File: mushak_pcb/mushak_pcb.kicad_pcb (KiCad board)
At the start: 2 copper layers, 57.7 x 40 mm, 115 parts, among them IC1 AS5600-ASOT, IC2 AS5600-ASOT, J1 Conn_01x04_Male, J10 IR_1, J11 AS5600_1, J12 IR_2, J13 AS5600_2, J14 IR_3, J15 ToF, J16 IR_4, J17 ToF, J2 Conn_01x02_Female, J3 BLE_Conn, J4 AS5600_Left, J5 AS5600_Right, J6 IR_1, J7 IR_3, J8 IR_2, J9 IR_4, M1 motor, M2 motor, Q1 DMN3065LW-7, Q2 DMN3065LW-7, Q3 DMN3065LW-7, Q4 DMN3065LW-7, Q5 DMN3065LW-7, SW1 SW_Push, SW2 SW_Push, U1 BA30BC0FP-E2, U3 DRV8833PW, U4 VL6180XV0NR/1, U5 MPU-6500, U6 STM32F405RGTx, Y1 25Mhz, Y2 32.769kHz

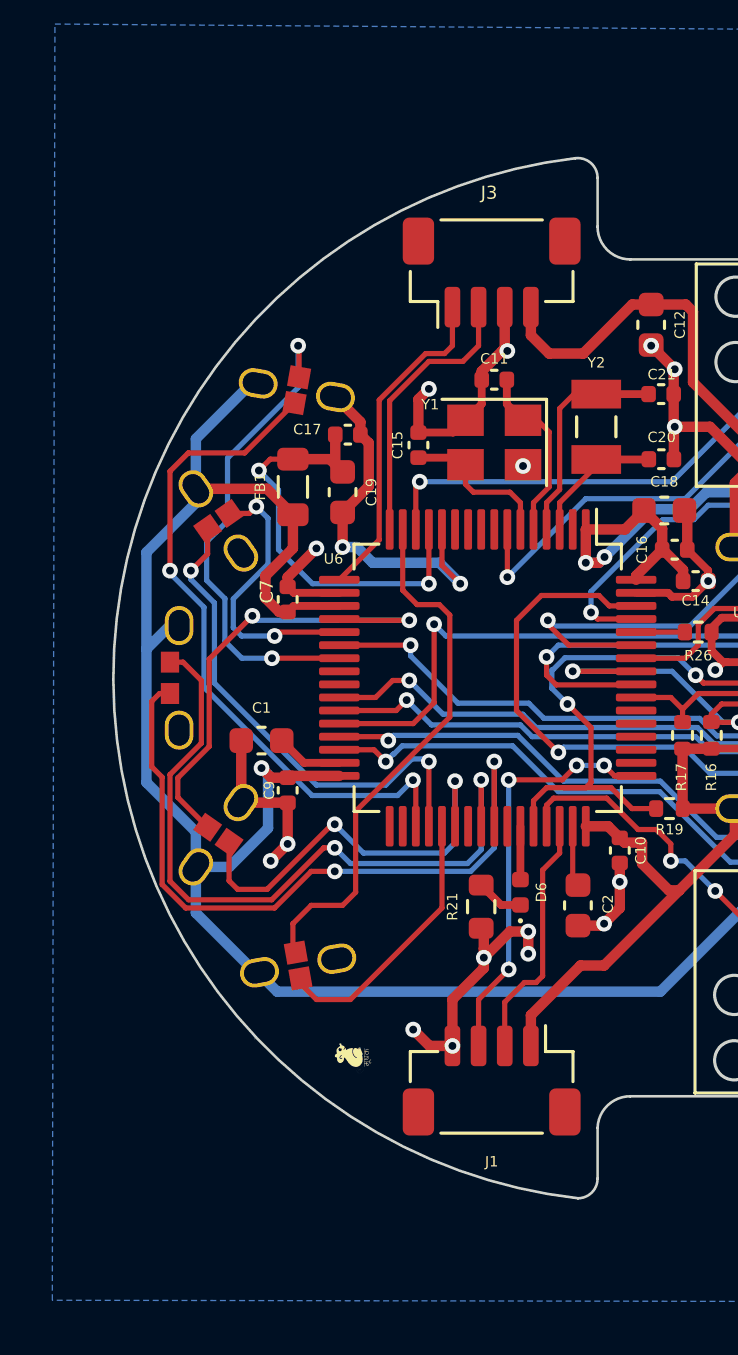
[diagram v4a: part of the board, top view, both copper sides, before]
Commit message: Updated graphics and added dimensions
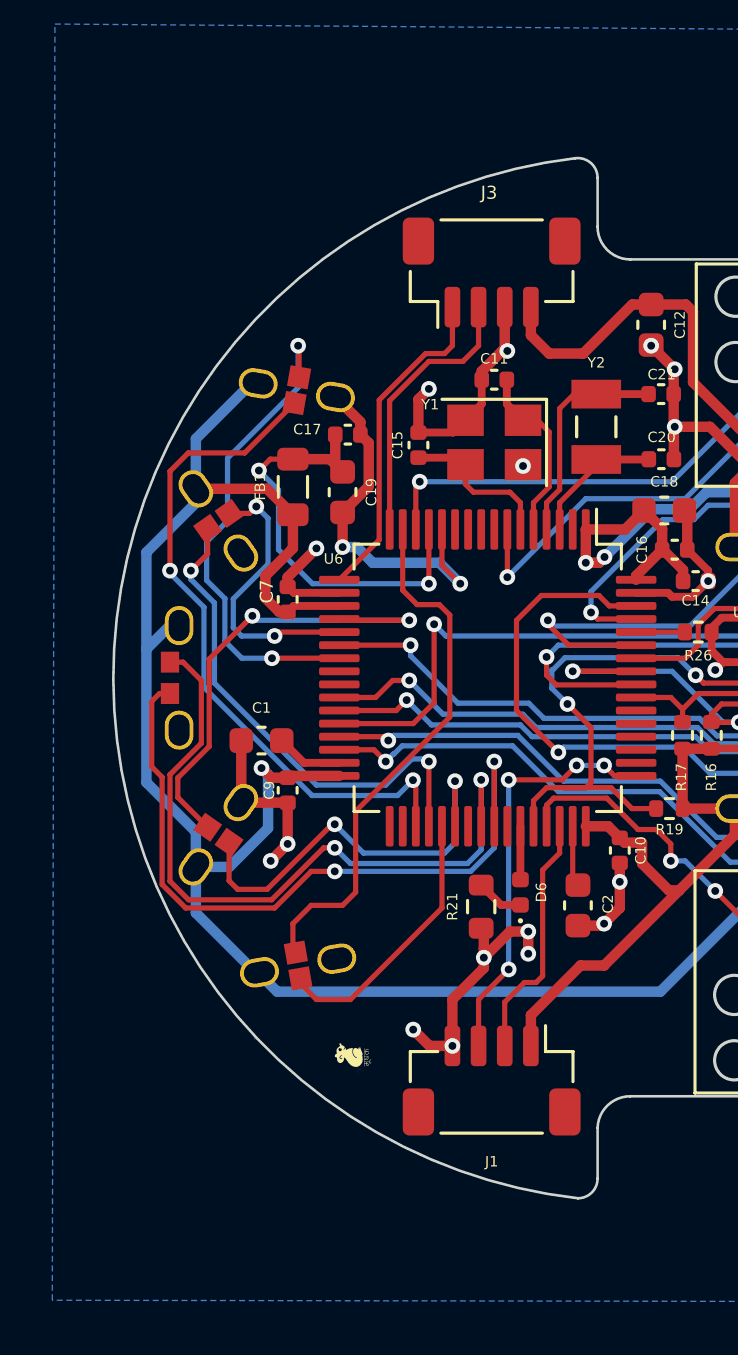
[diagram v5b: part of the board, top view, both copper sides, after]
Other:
- board text added: "SRA-VJTI"
- board text added: "Society of Robotics and Automation"
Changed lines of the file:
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@@
     (attr board_only exclude_from_pos_files exclude_from_bom)
     (fp_text reference "G***" (at 0.7 -3.75 90) (layer "F.SilkS")
-      (effects (font (size 0.05 0.05)))
+      (effects (font (size 0.05 0.05) (thickness 0.15)))
     )
     (fp_text value "LOGO" (at 0.75 0 90) (layer "F.SilkS") hide
@@
     (pad "8" smd rect locked (at 2.7 -1.905) (size 1.5 0.65) (layers "F.Cu" "F.Paste" "F.Mask")
       (net 18 "/AS5600_Right/GND_s") (pinfunction "DIR") (pintype "bidirectional"))
+    (model "${KIPRJMOD}/3d_models/AS5600/AS5600.stp"
+      (offset (xyz 0 0 0))
+      (scale (xyz 1 1 1))
+      (rotate (xyz 0 0 0))
+    )
   )
   (footprint "Capacitor_SMD:C_0402_1005Metric" (layer "F.Cu")
@@
       (net 100 "Net-(M1-Pad2)") (pinfunction "VMOT-") (pintype "input"))
     (model "${KIPRJMOD}/component_libraries/mushak_mount_footprint/L_Assem.STEP"
-      (offset (xyz 3 -36.5 -21))
+      (offset (xyz 3 -36.5 -21.5))
       (scale (xyz 1 1 1))
       (rotate (xyz -90 0 180))
@@
     (pad "8" smd rect locked (at 2.7 -1.905) (size 1.5 0.65) (layers "F.Cu" "F.Paste" "F.Mask")
       (net 31 "/AS5600_Left/+3V0_s") (pinfunction "DIR") (pintype "bidirectional"))
+    (model "${KIPRJMOD}/3d_models/AS5600/AS5600.stp"
+      (offset (xyz 0 0 0))
+      (scale (xyz 1 1 1))
+      (rotate (xyz 0 0 0))
+    )
   )
   (footprint "mushak_mount_footprint:IR_SLAVE_V_04" (layer "F.Cu")
@@
       (net 102 "Net-(M2-Pad2)") (pinfunction "VMOT-") (pintype "input"))
     (model "${KIPRJMOD}/component_libraries/mushak_mount_footprint/R_Assem.STEP"
-      (offset (xyz -29.5 -36.5 19.5))
+      (offset (xyz -29.5 -36.5 20.5))
       (scale (xyz 1 1 1))
       (rotate (xyz 90 0 0))
@@
   (gr_line (start 205.85 106.85) (end 204.75 106.85) (layer "Edge.Cuts") (width 0.1))
   (gr_line (start 204.85 112) (end 204.85 111.4) (layer "Edge.Cuts") (width 0.1))
-  (gr_arc (start 166 116.9) (mid 148.233702 97.059712) (end 165.9 77.13033) (layer "Edge.Cuts") (width 0.1))
+  (gr_arc (start 166 116.9) (mid 148.233259 97.059714) (end 165.9 77.13033) (layer "Edge.Cuts") (width 0.1))
   (gr_line (start 205.35 112.4) (end 205.35 115.2) (layer "Edge.Cuts") (width 0.1))
   (gr_line (start 205.4 98.8) (end 205.4 96.9) (layer "Edge.Cuts") (width 0.1))
@@
   (gr_line (start 206 65) (end 142.5 1.5) (layer "User.4") (width 0.15))
   (gr_line (start 142.5 128.5) (end 79 192) (layer "User.4") (width 0.15))
+  (gr_text "Society of Robotics and Automation" (at 186.15 97.65 90) (layer "B.SilkS")
+    (effects (font (size 0.7 0.7) (thickness 0.1)) (justify mirror))
+  )
   (gr_text "Designed by - Chinmay Lonkar" (at 190.9 96.6 90) (layer "B.SilkS")
     (effects (font (size 0.6 0.6) (thickness 0.08)) (justify mirror))
   )
+  (gr_text "SRA-VJTI" (at 188.65 97.05 90) (layer "B.SilkS")
+    (effects (font (size 1 1) (thickness 0.25)) (justify mirror))
+  )
+  (dimension (type aligned) (layer "Eco2.User")
+    (pts (xy 192.828427 78.171573) (xy 190 81))
+    (height 7.495331)
+    (gr_text "4.0000 mm" (at 185.301042 73.472614 45) (layer "Eco2.User")
+      (effects (font (size 1 1) (thickness 0.15)))
+    )
+    (format (units 3) (units_format 1) (precision 4))
+    (style (thickness 0.15) (arrow_length 1.27) (text_position_mode 0) (extension_height 0.58642) (extension_offset 0.5) keep_text_aligned)
+  )
+  (dimension (type aligned) (layer "Eco2.User")
+    (pts (xy 194 97) (xy 148.233702 97.059712))
+    (height 25.057386)
+    (gr_text "45.7663 mm" (at 171.082658 70.822492 0.07475465123) (layer "Eco2.User")
+      (effects (font (size 1 1) (thickness 0.15)))
+    )
+    (format (units 3) (units_format 1) (precision 4))
+    (style (thickness 0.15) (arrow_length 1.27) (text_position_mode 0) (extension_height 0.58642) (extension_offset 0.5) keep_text_aligned)
+  )
+  (dimension (type aligned) (layer "Eco2.User")
+    (pts (xy 148.233259 97.059714) (xy 168.3 97))
+    (height 26.007919)
+    (gr_text "20.0668 mm" (at 158.3406 121.887666 0.1704985503) (layer "Eco2.User")
+      (effects (font (size 1 1) (thickness 0.15)))
+    )
+    (format (units 3) (units_format 1) (precision 4))
+    (style (thickness 0.15) (arrow_length 1.27) (text_position_mode 0) (extension_height 0.58642) (extension_offset 0.5) keep_text_aligned)
+  )
+  (dimension (type aligned) (layer "Eco2.User")
+    (pts (xy 177.075 87.425) (xy 194 87.4))
+    (height -24.400859)
+    (gr_text "16.9250 mm" (at 185.499758 61.861669 0.08463181365) (layer "Eco2.User")
+      (effects (font (size 1 1) (thickness 0.15)))
+    )
+    (format (units 3) (units_format 1) (precision 4))
+    (style (thickness 0.15) (arrow_length 1.27) (text_position_mode 0) (extension_height 0.58642) (extension_offset 0.5) keep_text_aligned)
+  )
+  (dimension (type aligned) (layer "Eco2.User")
+    (pts (xy 177.075 86.925) (xy 182.575 86.925))
+    (height -17.975)
+    (gr_text "5.5000 mm" (at 179.825 67.8) (layer "Eco2.User")
+      (effects (font (size 1 1) (thickness 0.15)))
+    )
+    (format (units 3) (units_format 1) (precision 4))
+    (style (thickness 0.15) (arrow_length 1.27) (text_position_mode 0) (extension_height 0.58642) (extension_offset 0.5) keep_text_aligned)
+  )
+  (dimension (type aligned) (layer "Eco2.User")
+    (pts (xy 166.494225 77.313541) (xy 165.9941 77.8803))
+    (height 4.543301)
+    (gr_text "0.7559 mm" (at 161.975273 73.829925 48.57386691) (layer "Eco2.User")
+      (effects (font (size 1 1) (thickness 0.15)))
+    )
+    (format (units 3) (units_format 1) (precision 4))
+    (style (thickness 0.15) (arrow_length 1.27) (text_position_mode 0) (extension_height 0.58642) (extension_offset 0.5) keep_text_aligned)
+  )
+  (dimension (type aligned) (layer "Eco2.User")
+    (pts (xy 166.75 79.6) (xy 181.25 79.6))
+    (height -5.05)
+    (gr_text "14.5000 mm" (at 174 73.4) (layer "Eco2.User")
+      (effects (font (size 1 1) (thickness 0.15)))
+    )
+    (format (units 3) (units_format 1) (precision 4))
+    (style (thickness 0.15) (arrow_length 1.27) (text_position_mode 0) (extension_height 0.58642) (extension_offset 0.5) keep_text_aligned)
+  )
+  (dimension (type aligned) (layer "Eco2.User")
+    (pts (xy 186 77) (xy 186 117))
+    (height -28)
+    (gr_text "40.0000 mm" (at 212.85 97 90) (layer "Eco2.User")
+      (effects (font (size 1 1) (thickness 0.15)))
+    )
+    (format (units 3) (units_format 1) (precision 4))
+    (style (thickness 0.15) (arrow_length 1.27) (text_position_mode 0) (extension_height 0.58642) (extension_offset 0.5) keep_text_aligned)
+  )
   (segment (start 197.95 105.2) (end 196.15 103.4) (width 0.2) (layer "F.Cu") (net 1))

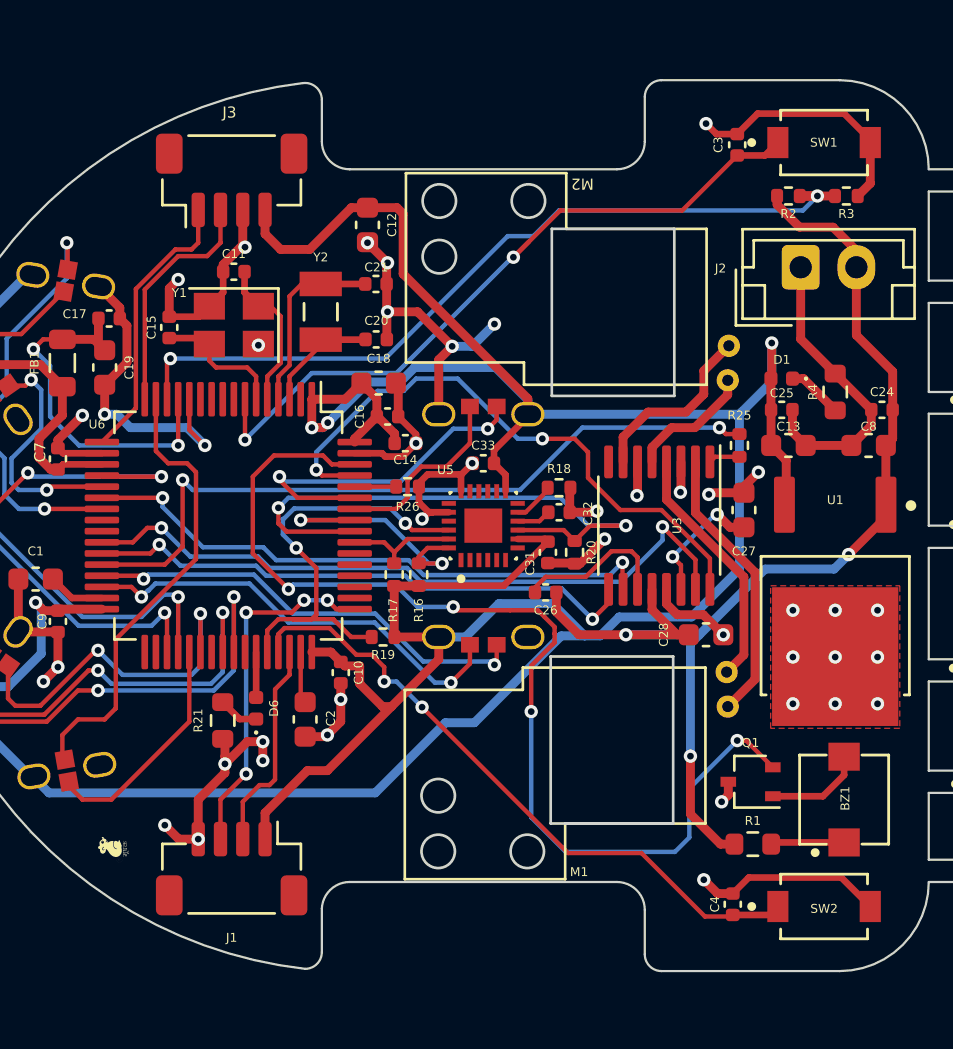
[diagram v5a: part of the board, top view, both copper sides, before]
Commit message: changed oscilattor placement
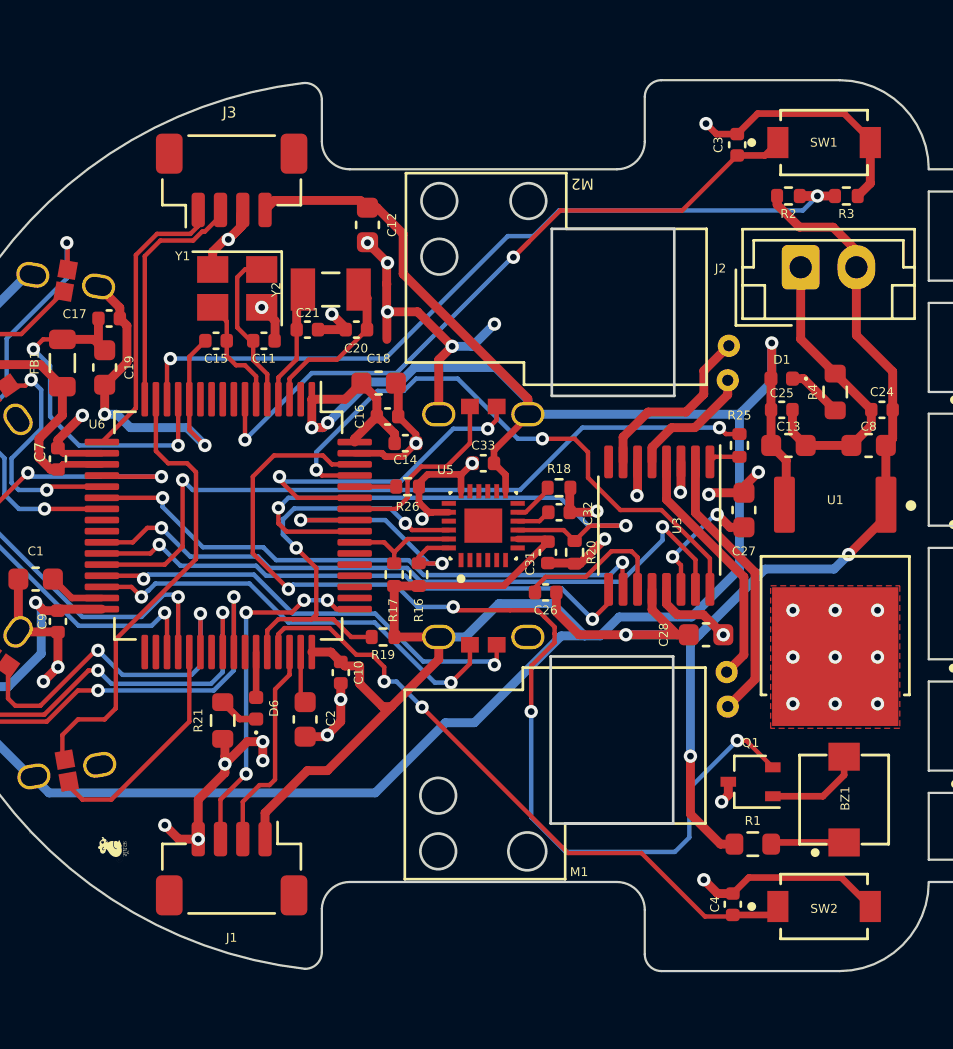
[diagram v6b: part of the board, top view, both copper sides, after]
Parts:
- added G***: LOGO, mushak_mount_footprint:open_harware, B.Cu at (162.8, 109.2)
- added G***: LOGO, mushak_mount_footprint:VJTI_Logo, B.Cu at (163.8, 85.4)
- moved C21 3.70 mm to (166.1, 88.2)
- moved C11 3.38 mm to (164.2, 88.7), turned to 0 degrees
- moved C15 2.18 mm to (162.0, 88.7), turned to 180 degrees
- moved Y1 1.66 mm to (162.9, 86.3)
- moved Y2 1.10 mm to (167.2, 86.4), turned to 180 degrees
- moved C20 0.99 mm to (168.3, 88.2), turned to 180 degrees
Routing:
- net Net-(C21-Pad1): track 8.46 -> 5.38 mm
- net POW_GND: track 123.1 -> 125.6 mm
- net +3V0: track 196.5 -> 194.2 mm
- net Net-(C20-Pad1): track 5.27 -> 7.27 mm
- net RCC_OSC_OUT: track 6.08 -> 5.17 mm
